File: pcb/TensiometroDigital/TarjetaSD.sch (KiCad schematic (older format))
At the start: 7 parts, among them J1 SD_Card

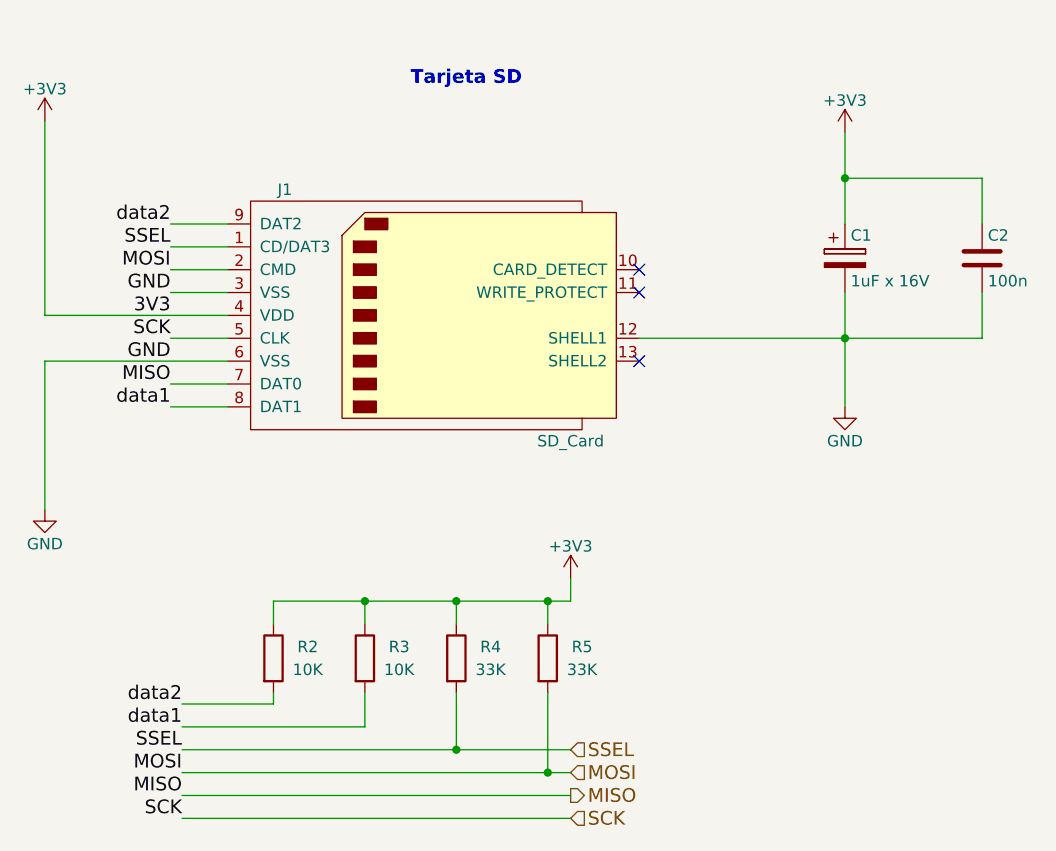
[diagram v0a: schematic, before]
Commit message: Finalizado: SCH, PCB, GABINETE, DRAWINGS. FALTA: GERBERS, BOM e Informe
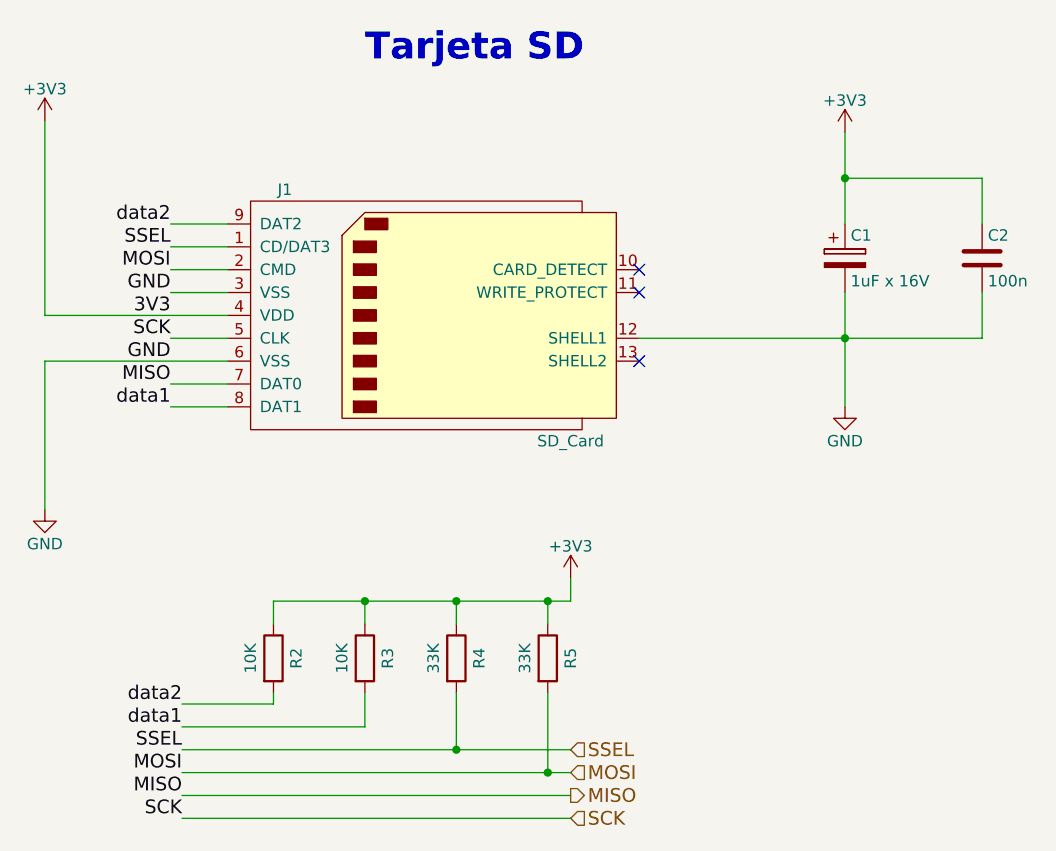
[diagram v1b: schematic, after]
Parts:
- C1: manf# (none) -> TMCP1C105MTRF
- C2: manf# (none) -> C0805X104J5RACAUTO
- J1: manf# (none) -> 2041021-3
- R2, R3: manf# (none) -> SG73G2ATTD1002D
- R4, R5: manf# (none) -> RT0805DRD0733KL
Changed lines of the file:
@@
 LIBS:lm2940
 LIBS:lm2575
+LIBS:bav199
+LIBS:mpxv5050gp
+LIBS:lm8364
 LIBS:TensiometroDigital-cache
 EELAYER 25 0
@@
 $Descr A4 11693 8268
 encoding utf-8
-Sheet 6 8
-Title "Tarjeta SD"
-Date "2018-09-10"
+Sheet 5 11
+Title "TENSIÓMETRO DIGITAL"
+Date "2018-11-20"
 Rev "A"
 Comp "UTN - FRBA"
-Comment1 ""
-Comment2 ""
-Comment3 ""
-Comment4 ""
+Comment1 "Curso: R1032"
+Comment2 "Leg.: 153204-2"
+Comment3 "Autor: Alegre Mendoza Ezequiel"
+Comment4 "SDR Proyecto Final"
 $EndDescr
 $Comp
@@
 F 2 "footprints:SD_TE_2041021_edit" H 5850 3350 50  0001 C CNN
 F 3 "" H 5650 3000 50  0001 C CNN
+F 4 "2041021-3" H 5650 3000 60  0001 C CNN "manf#"
 	1    5650 3000
 	1    0    0    -1
 $EndComp
 $Comp
-L +3V3 #PWR013
+L +3V3 #PWR015
 U 1 1 5B95F880
 P 3950 2150
-F 0 "#PWR013" H 3950 2000 50  0001 C CNN
+F 0 "#PWR015" H 3950 2000 50  0001 C CNN
 F 1 "+3V3" H 3950 2290 50  0000 C CNN
 F 2 "" H 3950 2150 50  0001 C CNN
@@
 $EndComp
 $Comp
-L GND #PWR014
+L GND #PWR016
 U 1 1 5B95F899
 P 3950 3850
-F 0 "#PWR014" H 3950 3600 50  0001 C CNN
+F 0 "#PWR016" H 3950 3600 50  0001 C CNN
 F 1 "GND" H 3950 3700 50  0000 C CNN
 F 2 "" H 3950 3850 50  0001 C CNN
@@
 F 2 "Capacitors_Tantalum_SMD:CP_Tantalum_Case-A_EIA-3216-18_Hand" H 7488 2600 50  0001 C CNN
 F 3 "" H 7450 2750 50  0001 C CNN
+F 4 "TMCP1C105MTRF" H 7450 2750 60  0001 C CNN "manf#"
 	1    7450 2750
 	1    0    0    -1
@@
 F 2 "Capacitors_SMD:C_0805_HandSoldering" H 8088 2600 50  0001 C CNN
 F 3 "" H 8050 2750 50  0001 C CNN
+F 4 "C0805X104J5RACAUTO" H 8050 2750 60  0001 C CNN "manf#"
 	1    8050 2750
 	1    0    0    -1
 $EndComp
 $Comp
-L +3V3 #PWR015
+L +3V3 #PWR017
 U 1 1 5B95FAF6
 P 7450 2200
-F 0 "#PWR015" H 7450 2050 50  0001 C CNN
+F 0 "#PWR017" H 7450 2050 50  0001 C CNN
 F 1 "+3V3" H 7450 2340 50  0000 C CNN
 F 2 "" H 7450 2200 50  0001 C CNN
@@
 $EndComp
 $Comp
-L GND #PWR016
+L GND #PWR018
 U 1 1 5B95FC27
 P 7450 3400
-F 0 "#PWR016" H 7450 3150 50  0001 C CNN
+F 0 "#PWR018" H 7450 3150 50  0001 C CNN
 F 1 "GND" H 7450 3250 50  0000 C CNN
 F 2 "" H 7450 3400 50  0001 C CNN
@@
 U 1 1 5B96095B
 P 4950 4500
-F 0 "R2" H 5100 4550 50  0000 C CNN
-F 1 "10K" H 5100 4450 50  0000 C CNN
+F 0 "R2" V 5050 4500 50  0000 C CNN
+F 1 "10K" V 4850 4500 50  0000 C CNN
 F 2 "Resistors_SMD:R_0805_HandSoldering" V 4880 4500 50  0001 C CNN
 F 3 "" H 4950 4500 50  0001 C CNN
+F 4 "SG73G2ATTD1002D " V 4950 4500 60  0001 C CNN "manf#"
 	1    4950 4500
 	1    0    0    -1
@@
 U 1 1 5B96098C
 P 5350 4500
-F 0 "R3" H 5500 4550 50  0000 C CNN
-F 1 "10K" H 5500 4450 50  0000 C CNN
+F 0 "R3" V 5450 4500 50  0000 C CNN
+F 1 "10K" V 5250 4500 50  0000 C CNN
 F 2 "Resistors_SMD:R_0805_HandSoldering" V 5280 4500 50  0001 C CNN
 F 3 "" H 5350 4500 50  0001 C CNN
+F 4 "SG73G2ATTD1002D " V 5350 4500 60  0001 C CNN "manf#"
 	1    5350 4500
 	1    0    0    -1
@@
 U 1 1 5B9609B5
 P 5750 4500
-F 0 "R4" H 5900 4550 50  0000 C CNN
-F 1 "33K" H 5900 4450 50  0000 C CNN
+F 0 "R4" V 5850 4500 50  0000 C CNN
+F 1 "33K" V 5650 4500 50  0000 C CNN
 F 2 "Resistors_SMD:R_0805_HandSoldering" V 5680 4500 50  0001 C CNN
 F 3 "" H 5750 4500 50  0001 C CNN
+F 4 "RT0805DRD0733KL" V 5750 4500 60  0001 C CNN "manf#"
 	1    5750 4500
 	1    0    0    -1
@@
 U 1 1 5B9609E0
 P 6150 4500
-F 0 "R5" H 6300 4550 50  0000 C CNN
-F 1 "33K" H 6300 4450 50  0000 C CNN
+F 0 "R5" V 6250 4500 50  0000 C CNN
+F 1 "33K" V 6050 4500 50  0000 C CNN
 F 2 "Resistors_SMD:R_0805_HandSoldering" V 6080 4500 50  0001 C CNN
 F 3 "" H 6150 4500 50  0001 C CNN
+F 4 "RT0805DRD0733KL" V 6150 4500 60  0001 C CNN "manf#"
 	1    6150 4500
 	1    0    0    -1
 $EndComp
 $Comp
-L +3V3 #PWR017
+L +3V3 #PWR019
 U 1 1 5B960A05
 P 6250 4150
-F 0 "#PWR017" H 6250 4000 50  0001 C CNN
+F 0 "#PWR019" H 6250 4000 50  0001 C CNN
 F 1 "+3V3" H 6250 4290 50  0000 C CNN
 F 2 "" H 6250 4150 50  0001 C CNN
@@
 Text HLabel 6250 5200 2    60   Input ~ 0
 SCK
-Text Notes 5550 2000 0    60   ~ 12
+Text Notes 5350 1900 0    118  ~ 24
 Tarjeta SD\n
 $EndSCHEMATC
